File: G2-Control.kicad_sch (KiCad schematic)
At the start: 95 parts, among them J1 Conn_01x06_Pin, J102 Conn_01x06_Pin, J103 Conn_01x06_Pin, J104 Board Interconnect, J2 Q2_link, J3 Conn_01x07_Pin, J4 Conn_01x05_Pin, K1 SMI-12VDC-SL-2C, K2 SMI-12VDC-SL-2C, K3 SMI-12VDC-SL-2C, Q1 TIP122, Q2 2SK3566, Q3 2N5061, Q4 2N4403, Q5 BC847, Q6 IRF9530N, U1 LM317L_SOT-89, U2 748, U3 4N36, U4 78L05, U5 LMC555CMX

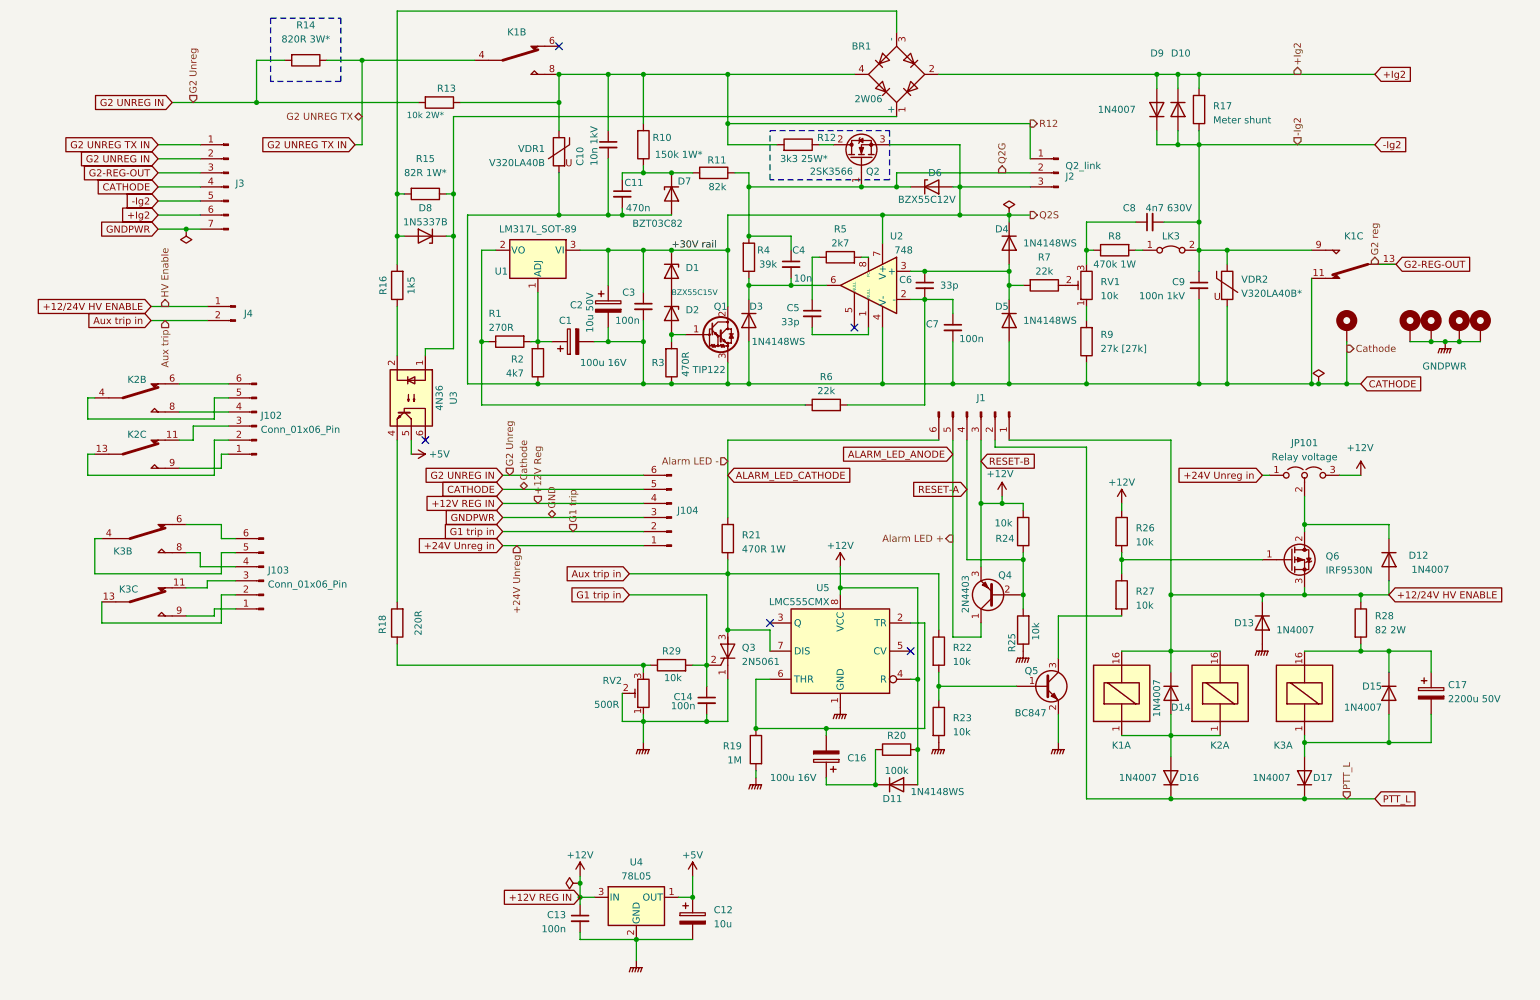
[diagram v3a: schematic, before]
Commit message: Replaced Q4 transistor schematic symbol BC557 with 2N3904 in G2-Control schematic
Updated the G2-Control schematic by replacing the schematic symbol BC557 for transistor Q4 with the symbol for 2N3904 which has the same pin numbering as the actual transistor used. This change fixes
issue #11 and makes the silkscreen print on the PCB show the transistor the way it has to be rotated in order to function properly.

Other changes is that the references and values of the components have been moved and the valye is set in a smaller font to increase readability. The global labels has also been replaced by hierarchical labels.
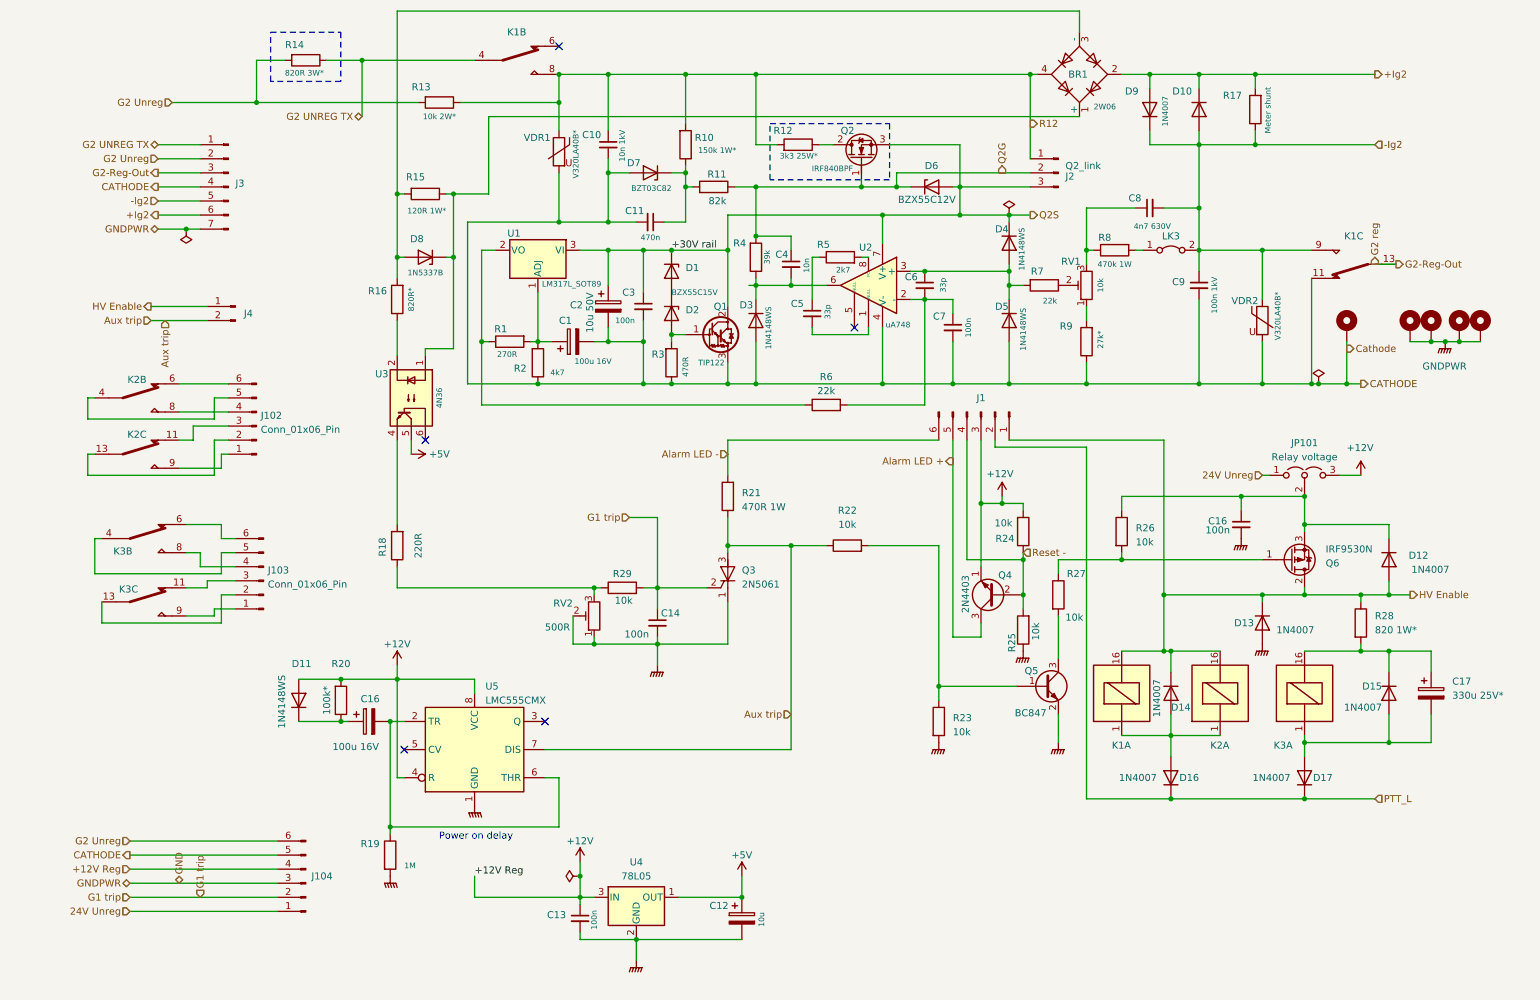
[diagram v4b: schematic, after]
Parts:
- added C16: 100n, Capacitor_SMD:C_1206_3216Metric, symbol Device:C_Small
- C17: value 2200u 50V -> 330u 25V*; Order # 41003415 -> (none); Supplier Electrokit -> Electrokit*
- Q2: value 2SK3566 -> IRF840BPF
- Q4: symbol Transistor_BJT:BC557 -> Transistor_BJT:2N3904
- R14: Order # KAL50FB1K00-ND -> KAL50FB1K00-ND*; Supplier DigiKey -> DigiKey*
- R15: value 82R 1W* -> 120R 1W*; Order # PPC82W-1CT-ND -> PPC82W-1CT-ND*; Supplier DigiKey -> DigiKey*
- R16: value 1k5 -> 820R*
- R20: value 100k -> 100k*
- R28: value 82 2W -> 820 1W*; Order # 82ZCT-ND -> (none); Supplier DigiKey -> (none)
- R9: value 27k [27k] -> 27k*
- U1: value LM317L_SOT-89 -> LM317L_SOT89
- U2: value 748 -> uA748
- VDR1: value V320LA40B -> V320LA40B*
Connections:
- net +12V: now also Q4.1 (E); no longer Q4.3 (E), R26.1
- net GNDPWR: now also C16.2
- net at D12.1 (K), JP101.2 (C): now also Q6.3 (S), R26.1, C16.1; no longer Q6.2 (D)
- net +12/24V HV ENABLE renamed HV Enable
- net HV Enable: now also Q6.2 (D); no longer Q6.3 (S)
- net +24V Unreg in renamed 24V Unreg
- net ALARM_LED_ANODE renamed Alarm LED +
- net Alarm LED +: now also Q4.3 (C); no longer Q4.1 (C)
- net ALARM_LED_CATHODE renamed Alarm LED -
- net Aux trip in renamed Aux trip
- net G1 trip in renamed G1 trip
- net G2 UNREG IN renamed G2 Unreg
- net G2 UNREG TX IN renamed G2 UNREG TX
- net G2-REG-OUT renamed G2 reg
- net RESET-A renamed Reset -
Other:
- note added: "Power on delay"
- moved on the sheet: BR1, C11, C12, C14, C16, C8, D10, D11, D3, D7, D8, D9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

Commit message: Updated relay components and adjusted wiring
The K1 relay has been updated from model AZ822-2C-24DSE to RTE24024 for better current handling in case of arc-over. Additionally, wiring for these components has been adjusted to fit the new model.
Moved R13 to a better location and increased its footprint.

Moved the grounding hole to a place near both the VDR2 and the connection to K1 in order to get as low as possible impedance to the cathode connection for these two components.
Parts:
- K1: value SMI-12VDC-SL-2C -> AZ822-2C-24DSE; footprint Relay_THT:Relay_DPDT_Omron_G5V-2 -> Relay_THT:Relay_DPDT_Schrack-RT2-FormC_RM5mm; symbol Relay:G5V-2_Split -> Relay:RTE2xxxx_split; Order # 41000606 -> 3385-AZ822-2C-24DSE-ND; Supplier Electrokit -> DigiKey
- K2: value SMI-12VDC-SL-2C -> AZ822-2C-24DSE; Order # 41000606 -> 3385-AZ822-2C-24DSE-ND; Supplier Electrokit -> DigiKey
- K3: value SMI-12VDC-SL-2C -> AZ822-2C-24DSE; Order # 41000606 -> (none); Supplier Electrokit -> (none)
- R13: footprint Resistor_THT:R_Axial_DIN0414_L11.9mm_D4.5mm_P5.08mm_Vertical -> Resistor_THT:R_Axial_Power_L20.0mm_W6.4mm_P7.62mm_Vertical
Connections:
- net -Ig2: now also K1.14; no longer K1.9
- net CATHODE: now also J3.2 (Pin_2), K1.12; no longer J3.4 (Pin_4), K1.11
- net G2 UNREG TX: now also J3.4 (Pin_4), K1.21; no longer J3.1 (Pin_1), K1.4
- net G2 Unreg: now also J3.1 (Pin_1); no longer J3.2 (Pin_2)
- net G2 reg: now also K1.11; no longer J3.3 (Pin_3), K1.13
- net HV Enable: now also K1.A1; no longer K1.16
- net R12: now also K1.24; no longer K1.8
- net at D14.2 (A), D16.2 (A), K2.1: now also K1.A2; no longer K1.1
- new net G2-Reg: J3.3 (Pin_3)
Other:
- moved on the sheet: K1B, K1C

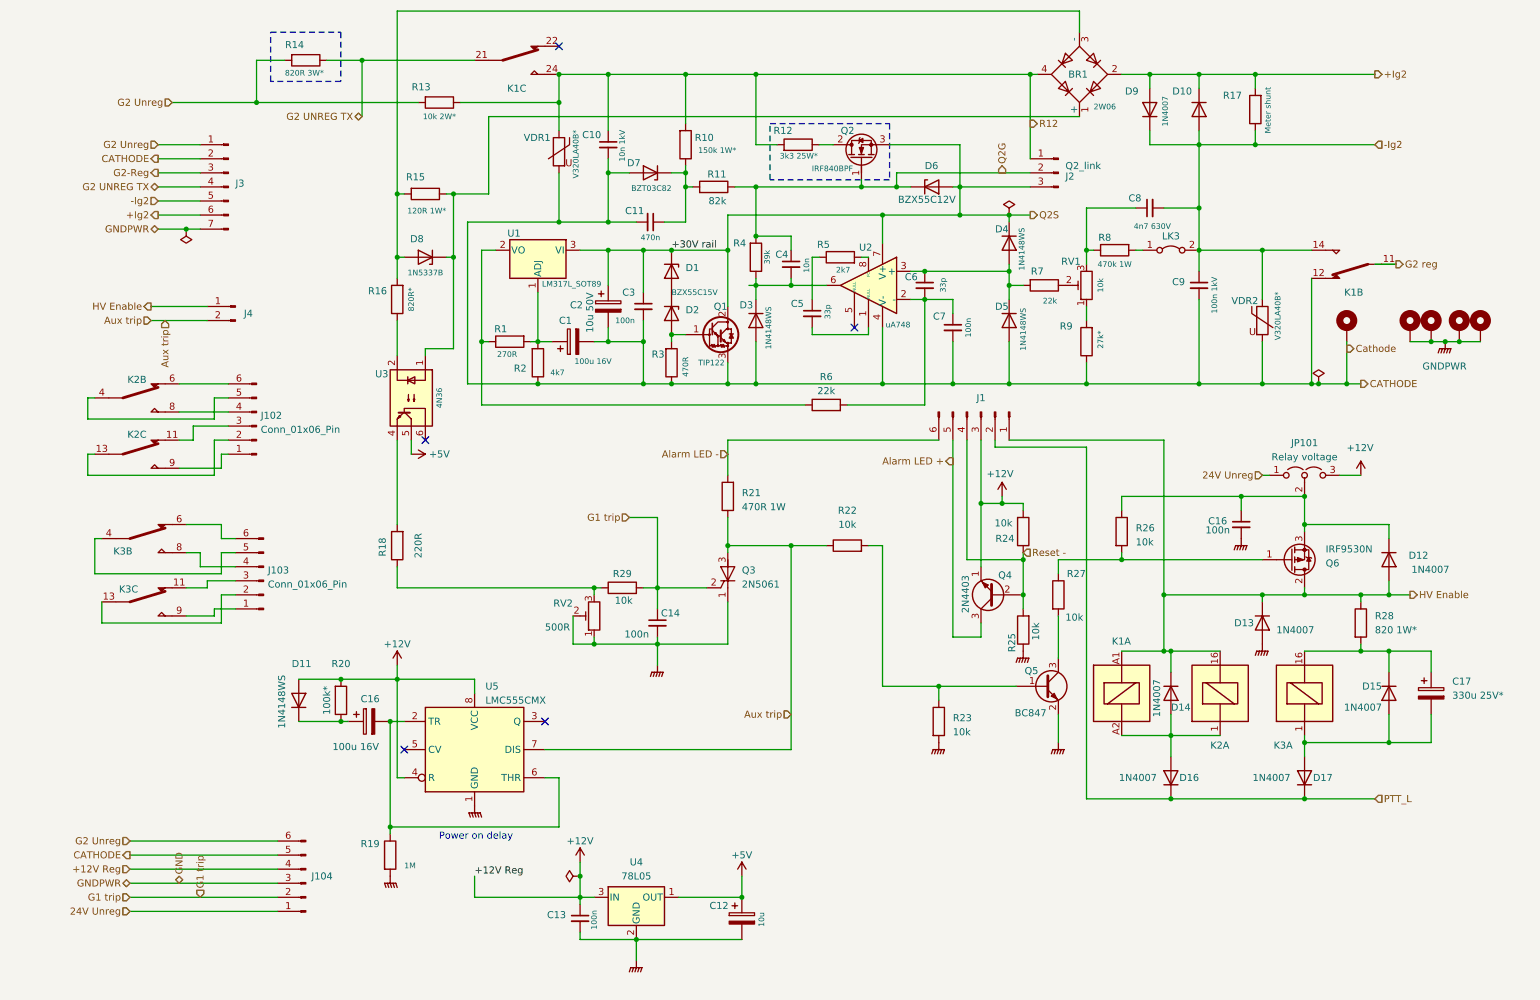
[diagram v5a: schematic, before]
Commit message: Updated capacitor C17. With the smaller relay and higher voltage, coil current is much less so 100 uF gives some 300-500 mS delay.
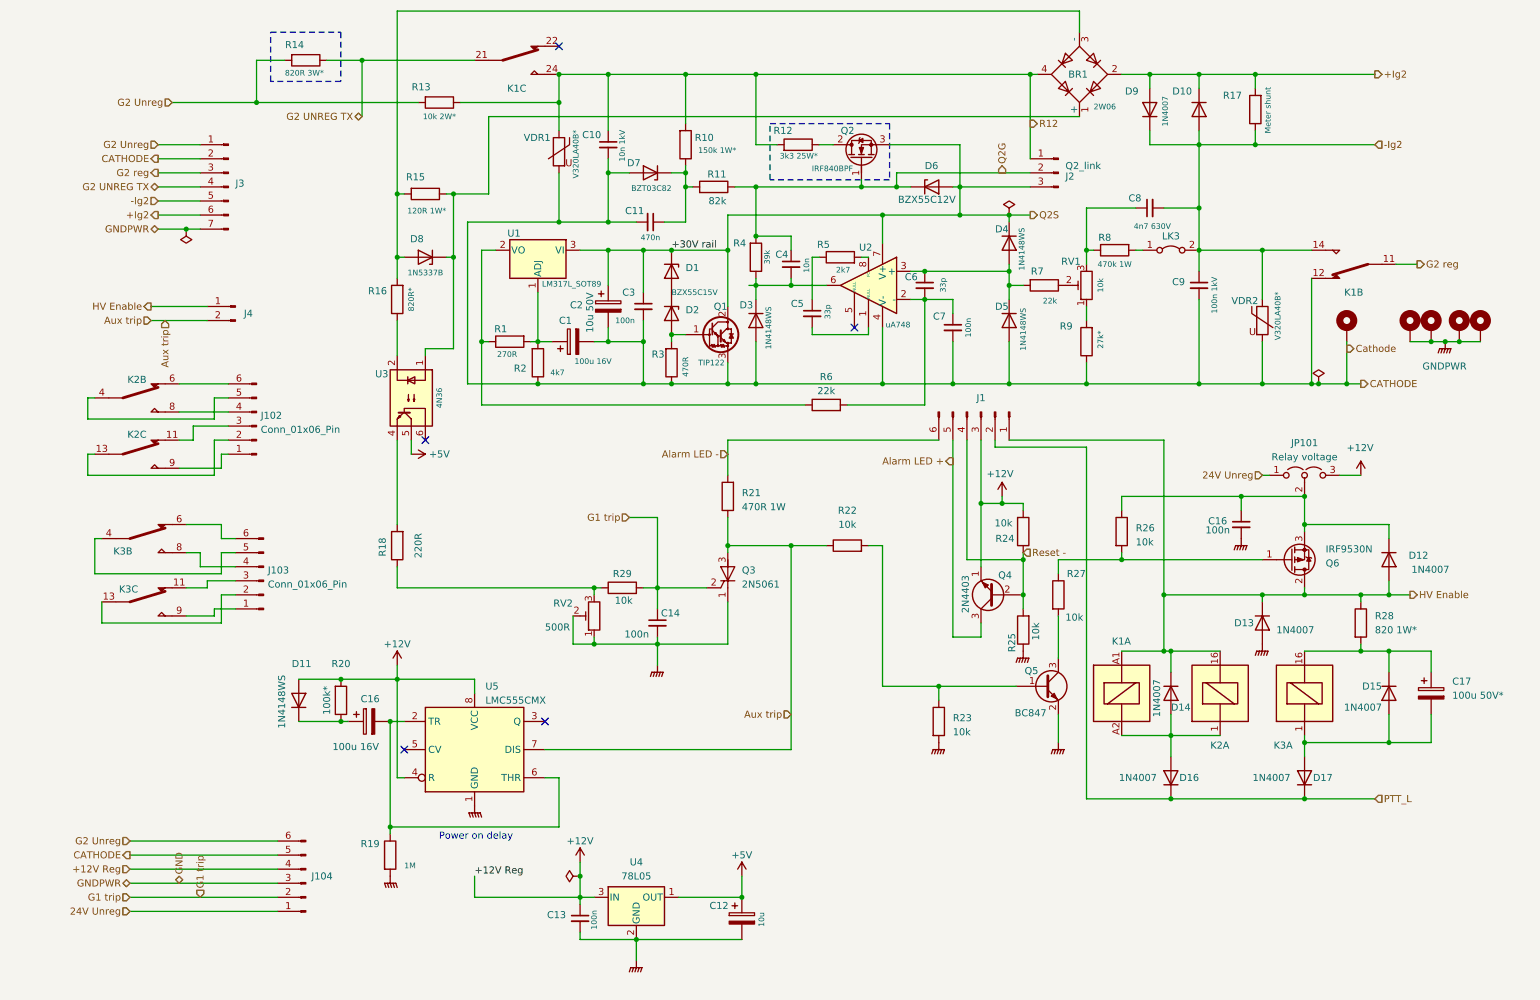
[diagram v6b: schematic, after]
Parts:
- C17: value 330u 25V* -> 100u 50V*; footprint Capacitor_THT:CP_Radial_D18.0mm_P7.50mm -> Capacitor_THT:CP_Radial_D8.0mm_P3.50mm
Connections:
- net G2-Reg is gone; now on net G2 reg: J3.3 (Pin_3)
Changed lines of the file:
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@@
 	(wire
 		(pts
-			(xy 260.35 60.96) (xy 264.16 60.96)
-		)
-		(stroke
-			(width 0)
-			(type default)
-		)
-	)
-	(wire
-		(pts
 			(xy 116.84 182.88) (xy 127 182.88)
 		)
@@
 	(wire
 		(pts
+			(xy 267.97 60.96) (xy 264.16 60.96)
+		)
+		(stroke
+			(width 0)
+			(type default)
+		)
+	)
+	(wire
+		(pts
 			(xy 130.81 119.38) (xy 139.7 119.38)
 		)
@@
 	(hierarchical_label "G2 reg"
 		(shape output)
-		(at 264.16 60.96 0)
+		(at 267.97 60.96 0)
 		(fields_autoplaced yes)
 		(effects
@@
 		)
 	)
-	(hierarchical_label "G2-Reg"
+	(hierarchical_label "G2 reg"
 		(shape output)
 		(at 40.64 44.45 180)
@@
 		(length 2.54)
 		(shape round)
-		(at 264.16 60.96 0)
+		(at 267.97 60.96 0)
 		(effects
 			(font
@@
 		)
 		(property "Netclass" "HVDC"
-			(at 270.51 58.42 0)
+			(at 274.32 58.42 0)
 			(effects
 				(font
@@
 			)
 		)
-		(property "Value" "330u 25V*"
+		(property "Value" "100u 50V*"
 			(at 274.32 138.8109 0)
 			(effects
@@
 			)
 		)
-		(property "Footprint" "Capacitor_THT:CP_Radial_D18.0mm_P7.50mm"
+		(property "Footprint" "Capacitor_THT:CP_Radial_D8.0mm_P3.50mm"
 			(at 271.4752 142.24 0)
 			(effects
